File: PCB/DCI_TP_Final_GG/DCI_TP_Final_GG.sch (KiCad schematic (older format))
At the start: 0 parts

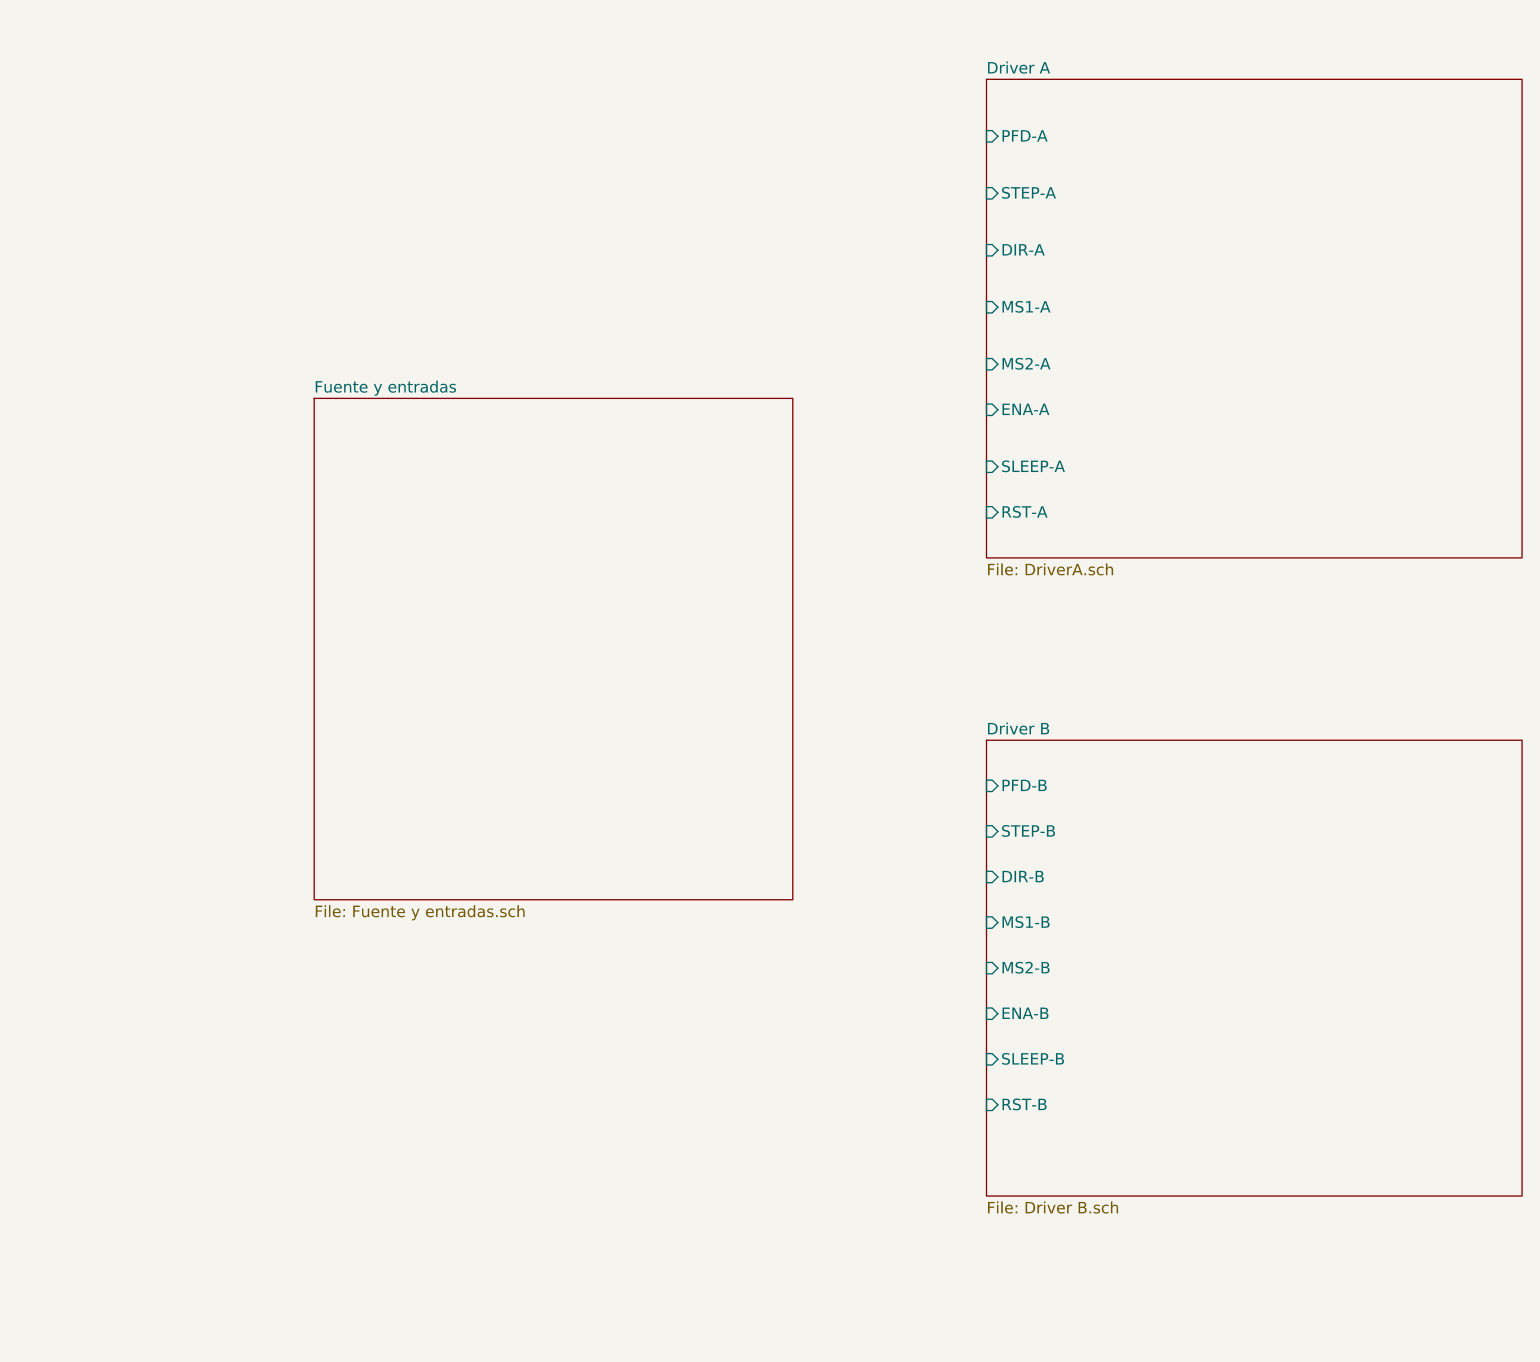
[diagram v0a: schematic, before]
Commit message: Agrego esquematico de fuente (falta completar)
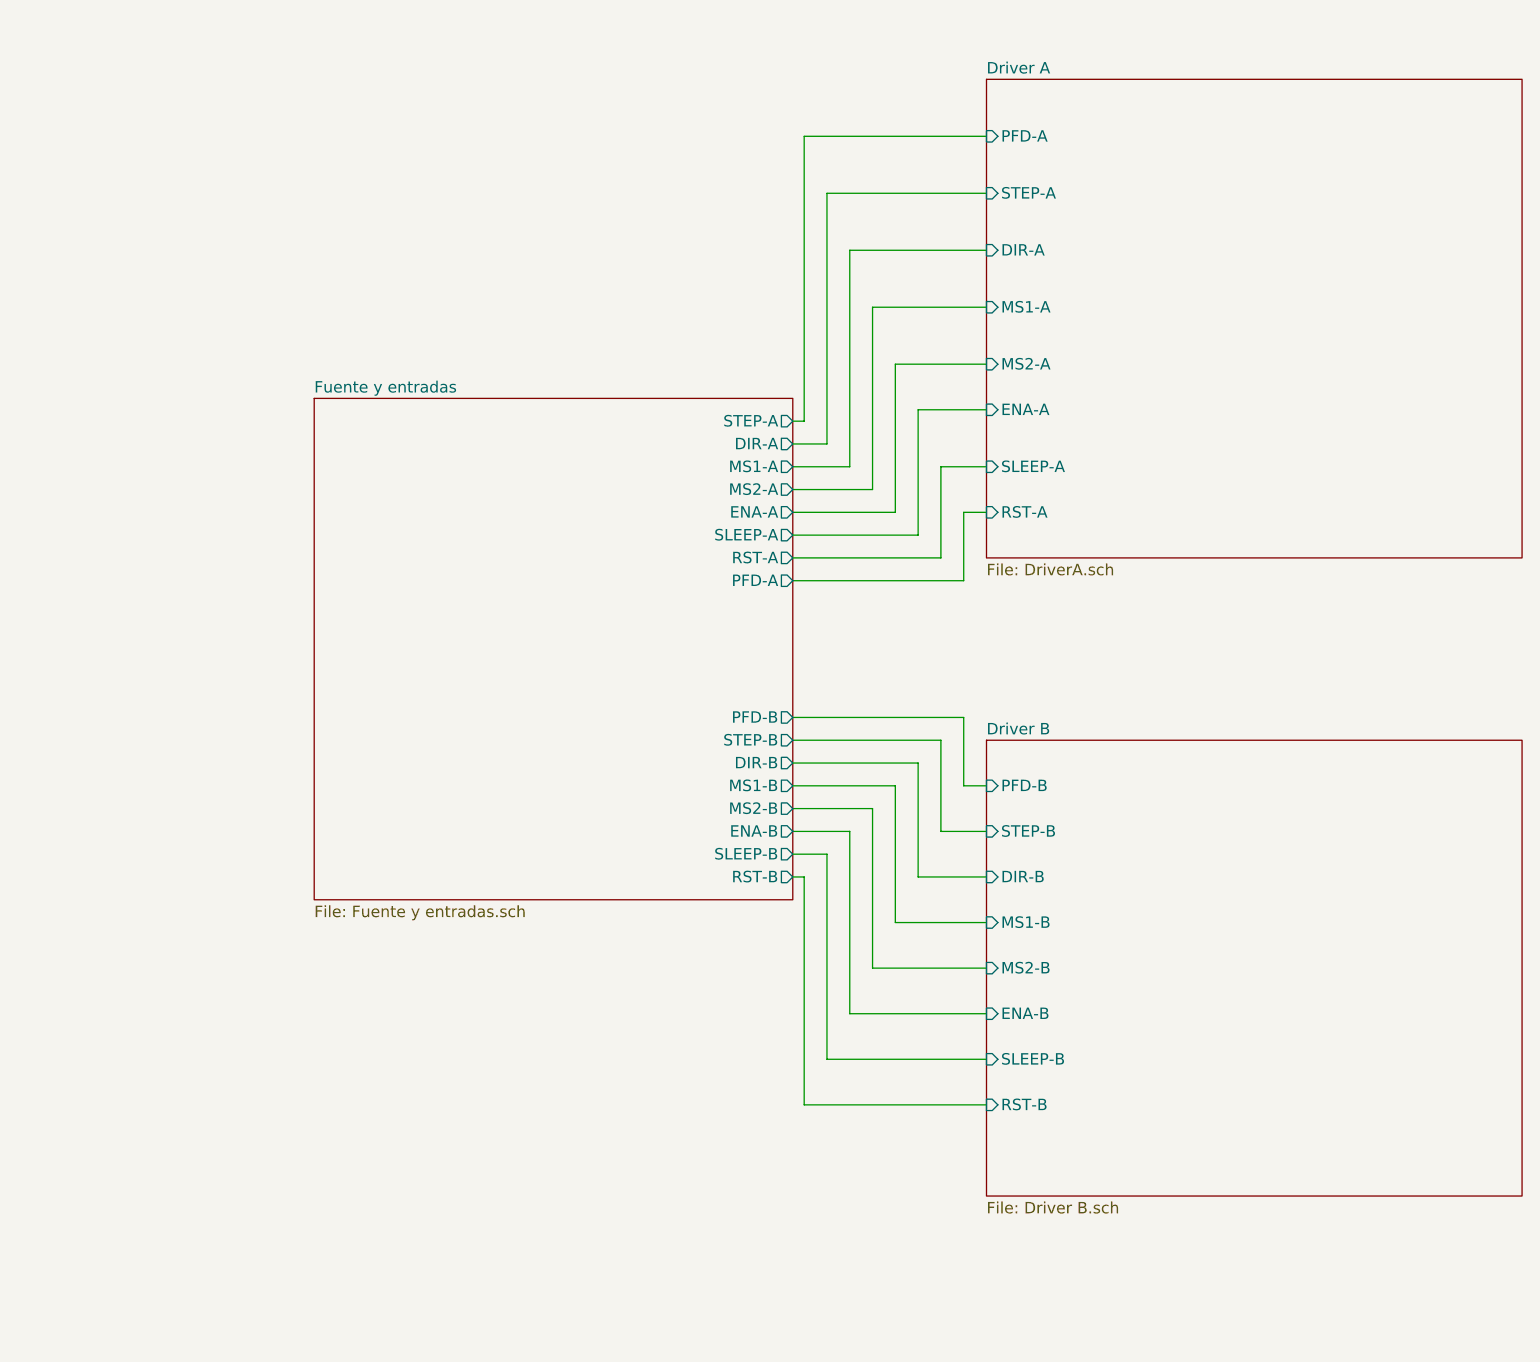
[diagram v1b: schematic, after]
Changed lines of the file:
@@
 F0 "Fuente y entradas" 50
 F1 "Fuente y entradas.sch" 50
+F2 "MS1-A" O R 4800 2800 50
+F3 "MS2-A" O R 4800 2900 50
+F4 "ENA-A" O R 4800 3000 50
+F5 "SLEEP-A" O R 4800 3100 50
+F6 "RST-A" O R 4800 3200 50
+F7 "STEP-A" O R 4800 2600 50
+F8 "DIR-A" O R 4800 2700 50
+F9 "PFD-A" O R 4800 3300 50
+F10 "MS1-B" O R 4800 4200 50
+F11 "MS2-B" O R 4800 4300 50
+F12 "ENA-B" O R 4800 4400 50
+F13 "SLEEP-B" O R 4800 4500 50
+F14 "RST-B" O R 4800 4600 50
+F15 "STEP-B" O R 4800 4000 50
+F16 "DIR-B" O R 4800 4100 50
+F17 "PFD-B" O R 4800 3900 50
 $EndSheet
+Wire Wire Line
+	4800 3900 5550 3900
+Wire Wire Line
+	5550 3900 5550 4200
+Wire Wire Line
+	5550 4200 5650 4200
+Wire Wire Line
+	4800 4000 5450 4000
+Wire Wire Line
+	5450 4000 5450 4400
+Wire Wire Line
+	5450 4400 5650 4400
+Wire Wire Line
+	4800 4100 5350 4100
+Wire Wire Line
+	5350 4100 5350 4600
+Wire Wire Line
+	5350 4600 5650 4600
+Wire Wire Line
+	4800 4200 5250 4200
+Wire Wire Line
+	5250 4200 5250 4800
+Wire Wire Line
+	5250 4800 5650 4800
+Wire Wire Line
+	4800 4300 5150 4300
+Wire Wire Line
+	5150 4300 5150 5000
+Wire Wire Line
+	5150 5000 5650 5000
+Wire Wire Line
+	4800 4400 5050 4400
+Wire Wire Line
+	5050 4400 5050 5200
+Wire Wire Line
+	5050 5200 5650 5200
+Wire Wire Line
+	4800 4500 4950 4500
+Wire Wire Line
+	4950 4500 4950 5400
+Wire Wire Line
+	4950 5400 5650 5400
+Wire Wire Line
+	4800 4600 4850 4600
+Wire Wire Line
+	4850 4600 4850 5600
+Wire Wire Line
+	4850 5600 5650 5600
+Wire Wire Line
+	4800 3300 5550 3300
+Wire Wire Line
+	5550 3300 5550 3000
+Wire Wire Line
+	5550 3000 5650 3000
+Wire Wire Line
+	4800 3200 5450 3200
+Wire Wire Line
+	5450 3200 5450 2800
+Wire Wire Line
+	5450 2800 5650 2800
+Wire Wire Line
+	4800 3100 5350 3100
+Wire Wire Line
+	5350 3100 5350 2550
+Wire Wire Line
+	5350 2550 5650 2550
+Wire Wire Line
+	4800 3000 5250 3000
+Wire Wire Line
+	5250 3000 5250 2350
+Wire Wire Line
+	5250 2350 5650 2350
+Wire Wire Line
+	4800 2900 5150 2900
+Wire Wire Line
+	5150 2900 5150 2100
+Wire Wire Line
+	5150 2100 5650 2100
+Wire Wire Line
+	4800 2800 5050 2800
+Wire Wire Line
+	5050 2800 5050 1850
+Wire Wire Line
+	5050 1850 5650 1850
+Wire Wire Line
+	4800 2700 4950 2700
+Wire Wire Line
+	4950 2700 4950 1600
+Wire Wire Line
+	4950 1600 5650 1600
+Wire Wire Line
+	4800 2600 4850 2600
+Wire Wire Line
+	4850 2600 4850 1350
+Wire Wire Line
+	4850 1350 5650 1350
 $EndSCHEMATC

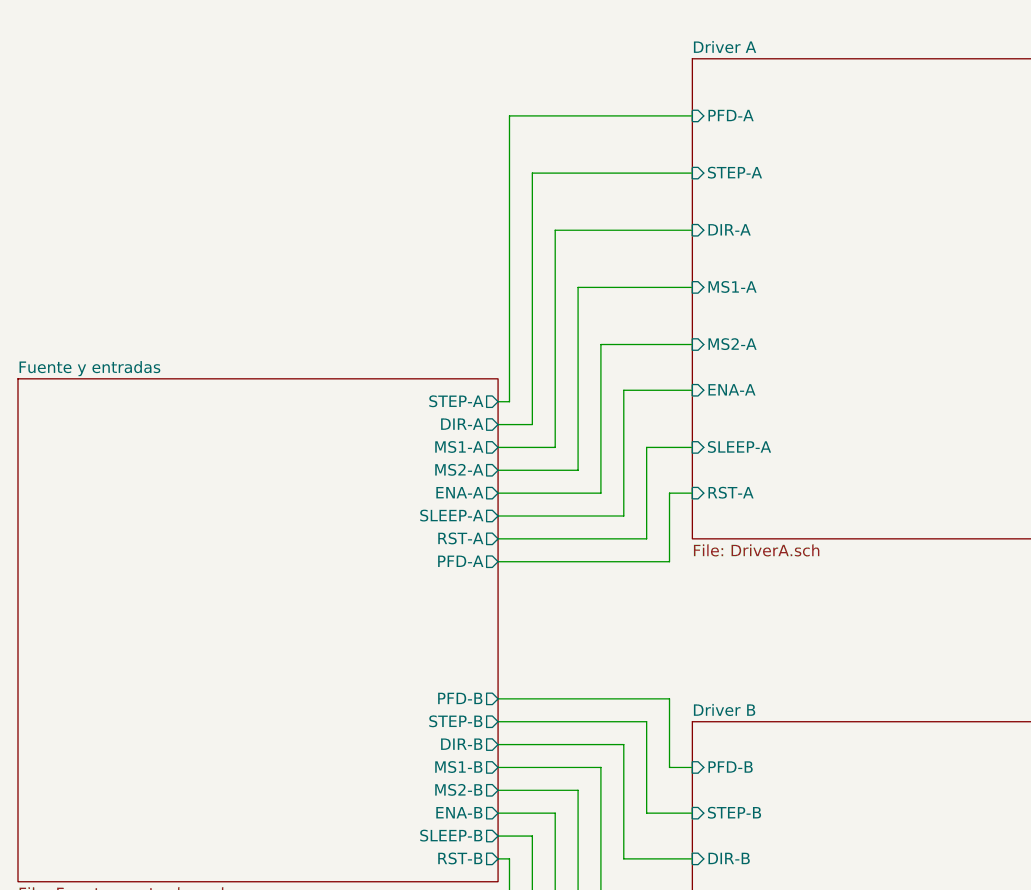
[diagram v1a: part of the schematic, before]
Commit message: Hoja de fuente y conectores completa.
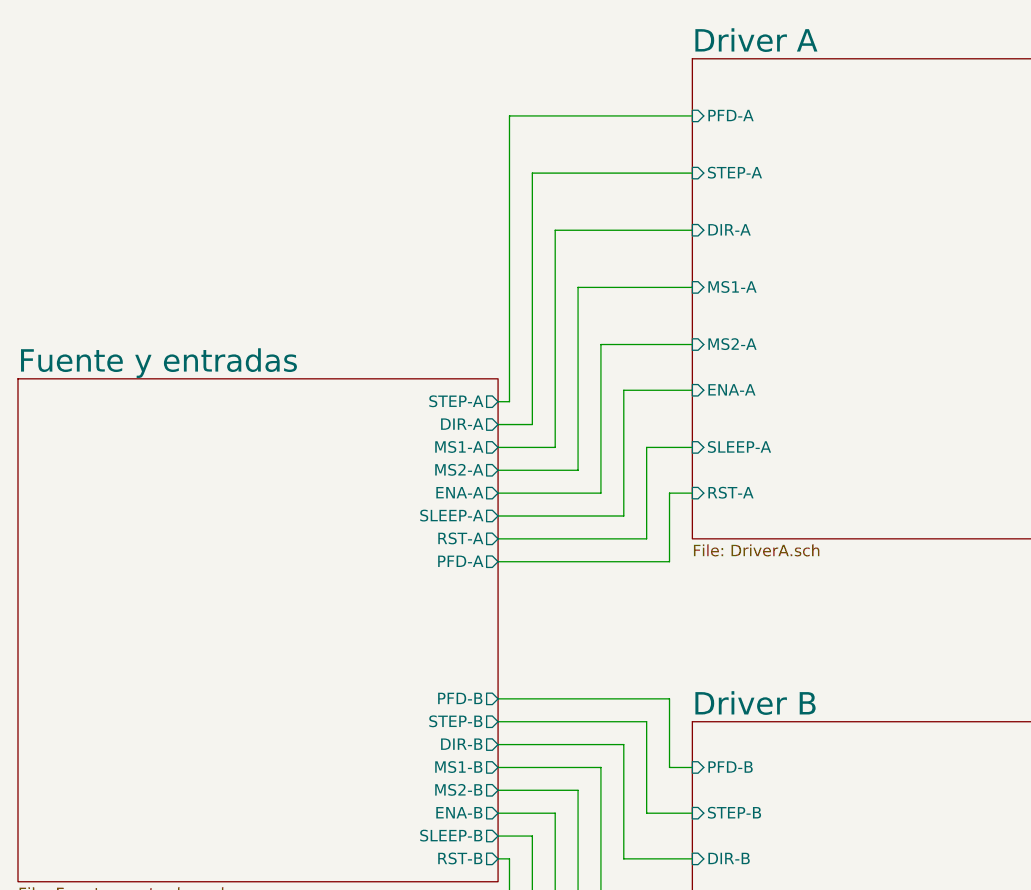
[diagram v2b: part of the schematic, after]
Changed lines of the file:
@@
 encoding utf-8
 Sheet 1 4
-Title "Replica EasyDriver v4.5"
+Title "Replica Dual EasyDriver v4.5"
 Date "2019-10-02"
 Rev ""
@@
 S 5650 1100 2350 2100
 U 5D9739A6
-F0 "Driver A" 50
+F0 "Driver A" 98
 F1 "DriverA.sch" 50
 F2 "PFD-A" I L 5650 1350 50
@@
 S 5650 4000 2350 2000
 U 5D9739FA
-F0 "Driver B" 50
+F0 "Driver B" 98
 F1 "Driver B.sch" 50
 F2 "PFD-B" I L 5650 4200 50
@@
 F8 "SLEEP-B" I L 5650 5400 50
 F9 "RST-B" I L 5650 5600 50
-$EndSheet
-$Sheet
-S 2700 2500 2100 2200
-U 5D973A64
-F0 "Fuente y entradas" 50
-F1 "Fuente y entradas.sch" 50
-F2 "MS1-A" O R 4800 2800 50
-F3 "MS2-A" O R 4800 2900 50
-F4 "ENA-A" O R 4800 3000 50
-F5 "SLEEP-A" O R 4800 3100 50
-F6 "RST-A" O R 4800 3200 50
-F7 "STEP-A" O R 4800 2600 50
-F8 "DIR-A" O R 4800 2700 50
-F9 "PFD-A" O R 4800 3300 50
-F10 "MS1-B" O R 4800 4200 50
-F11 "MS2-B" O R 4800 4300 50
-F12 "ENA-B" O R 4800 4400 50
-F13 "SLEEP-B" O R 4800 4500 50
-F14 "RST-B" O R 4800 4600 50
-F15 "STEP-B" O R 4800 4000 50
-F16 "DIR-B" O R 4800 4100 50
-F17 "PFD-B" O R 4800 3900 50
 $EndSheet
 Wire Wire Line
@@
 Wire Wire Line
 	4850 1350 5650 1350
+$Sheet
+S 2700 2500 2100 2200
+U 5D973A64
+F0 "Fuente y entradas" 98
+F1 "Fuente y entradas.sch" 50
+F2 "MS1-A" O R 4800 2800 50
+F3 "MS2-A" O R 4800 2900 50
+F4 "ENA-A" O R 4800 3000 50
+F5 "SLEEP-A" O R 4800 3100 50
+F6 "RST-A" O R 4800 3200 50
+F7 "STEP-A" O R 4800 2600 50
+F8 "DIR-A" O R 4800 2700 50
+F9 "PFD-A" O R 4800 3300 50
+F10 "MS1-B" O R 4800 4200 50
+F11 "MS2-B" O R 4800 4300 50
+F12 "ENA-B" O R 4800 4400 50
+F13 "SLEEP-B" O R 4800 4500 50
+F14 "RST-B" O R 4800 4600 50
+F15 "STEP-B" O R 4800 4000 50
+F16 "DIR-B" O R 4800 4100 50
+F17 "PFD-B" O R 4800 3900 50
+$EndSheet
 $EndSCHEMATC
